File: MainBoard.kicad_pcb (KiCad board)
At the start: 2 copper layers, 121.5 x 73.2 mm, 172 parts, among them J1 CONN_1x4, J10 CONN_2X2, J11 CONN_2X2, J17 HV, J18 CONN_1X2, J19 CONN_1X2, J2 CONN_2X3, J3 CONN_2X3, J4 CONN_2X2, J5 SWDEBUG_CONNECTOR, J6 CONN_2X2, J7 CONN_2X12, J8 CONN_1X2, J9 Micro_SD_Card_Det_Hirose_DM3AT, K1 KT12-1A, K2 G6DN 12V, Q1 SSM3K361TU,LF, Q2 TSM2312, SW1 RESET, U1 VX07805-1000, U10 DCDC_ISO_5V_ISO, U11 STM32G474, U12 M95M56-WMN6P, U13 TS3704IPT, U14 4044, U15 CD4082, U16 ADCMP350, U17 ADG706, U19 TCMT1103, U2 TPS2115A, U23 CD4072BPW, U24 LTC6259, U26 TCMT1103, U27 DCDC_ISO_5V, U28 MIC5365-3.3YC5, U29 Si8900, U3 ld1117s33, U30 MAX14878AWA+, U4 AD8244, U5 MCP2562, U6 LTC6259, U7 ADCMP354, U8 LTC6820, U9 HM2103

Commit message: added a lot of annotations and readability in the schematic, not complete
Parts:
- U12: value M95M56-WMN6P -> M95256-WMN6P
- U14: value 4044 -> CD4044
- U4: value AD8244 -> EL5421T

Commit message: Logo wasn't virtual, new netlist
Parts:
- renumbered G*** to G1, G*** to G2, G*** to G3, G*** to G4

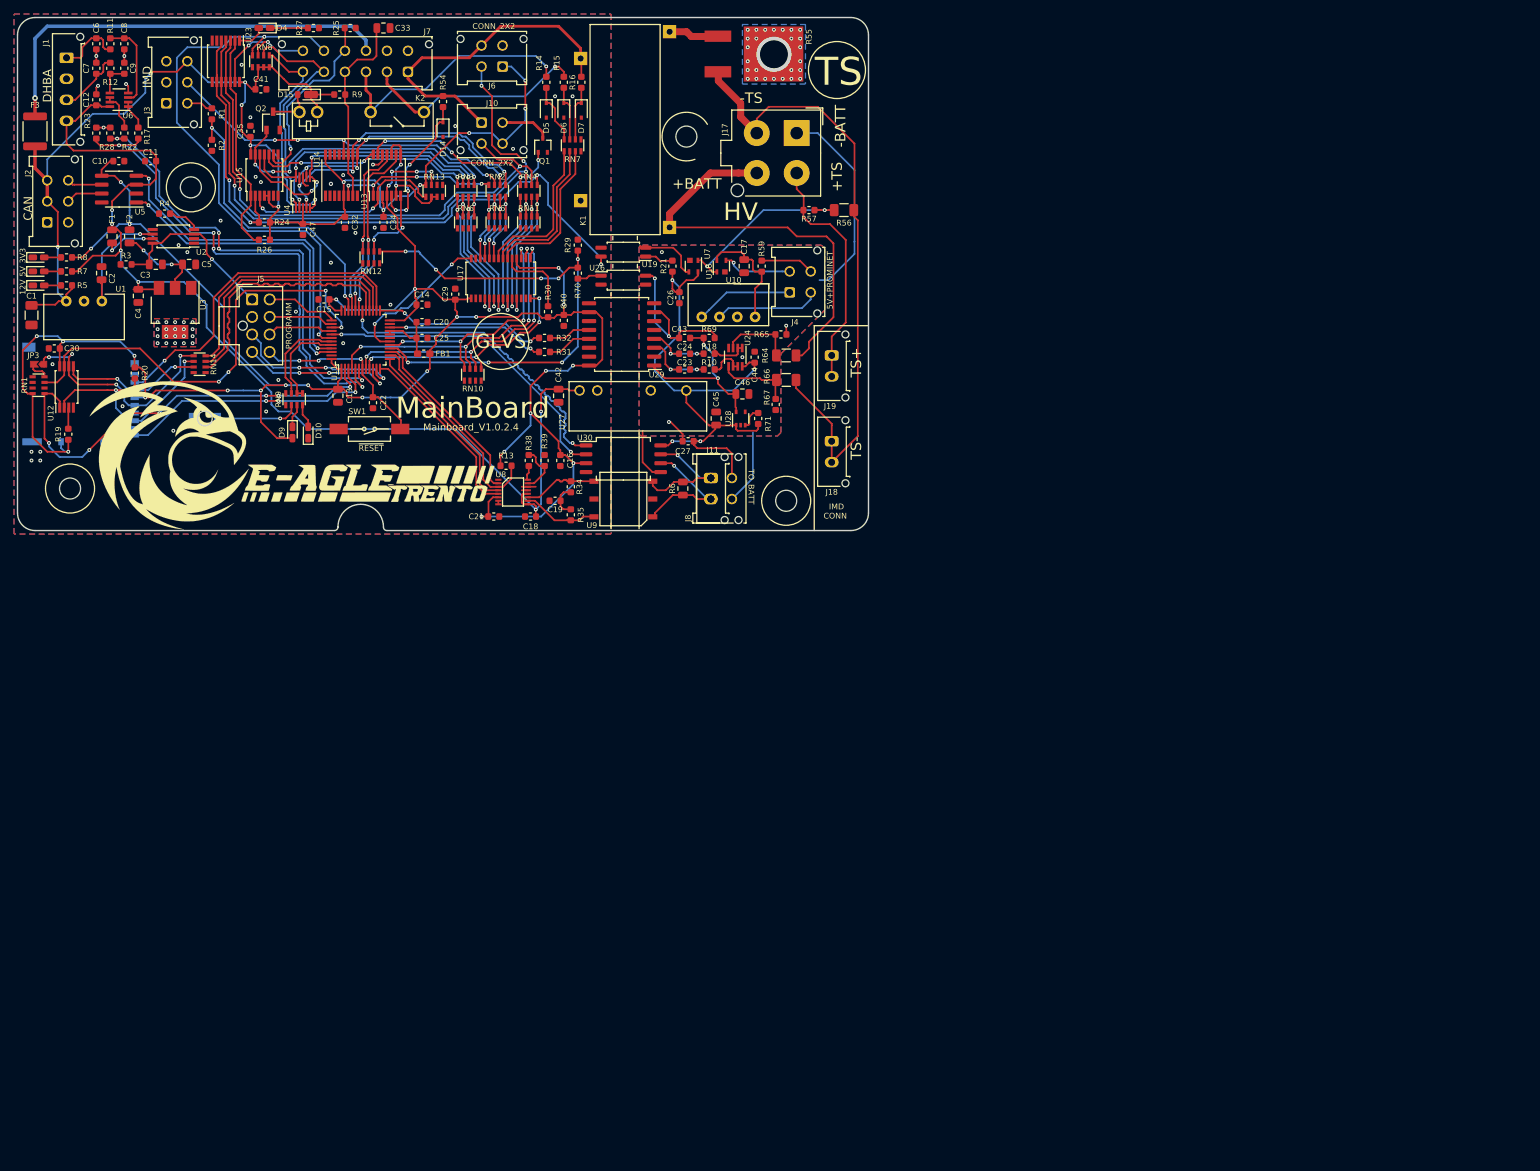
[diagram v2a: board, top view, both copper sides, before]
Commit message: Updated all to the last new v1.0.5 as printed by taba
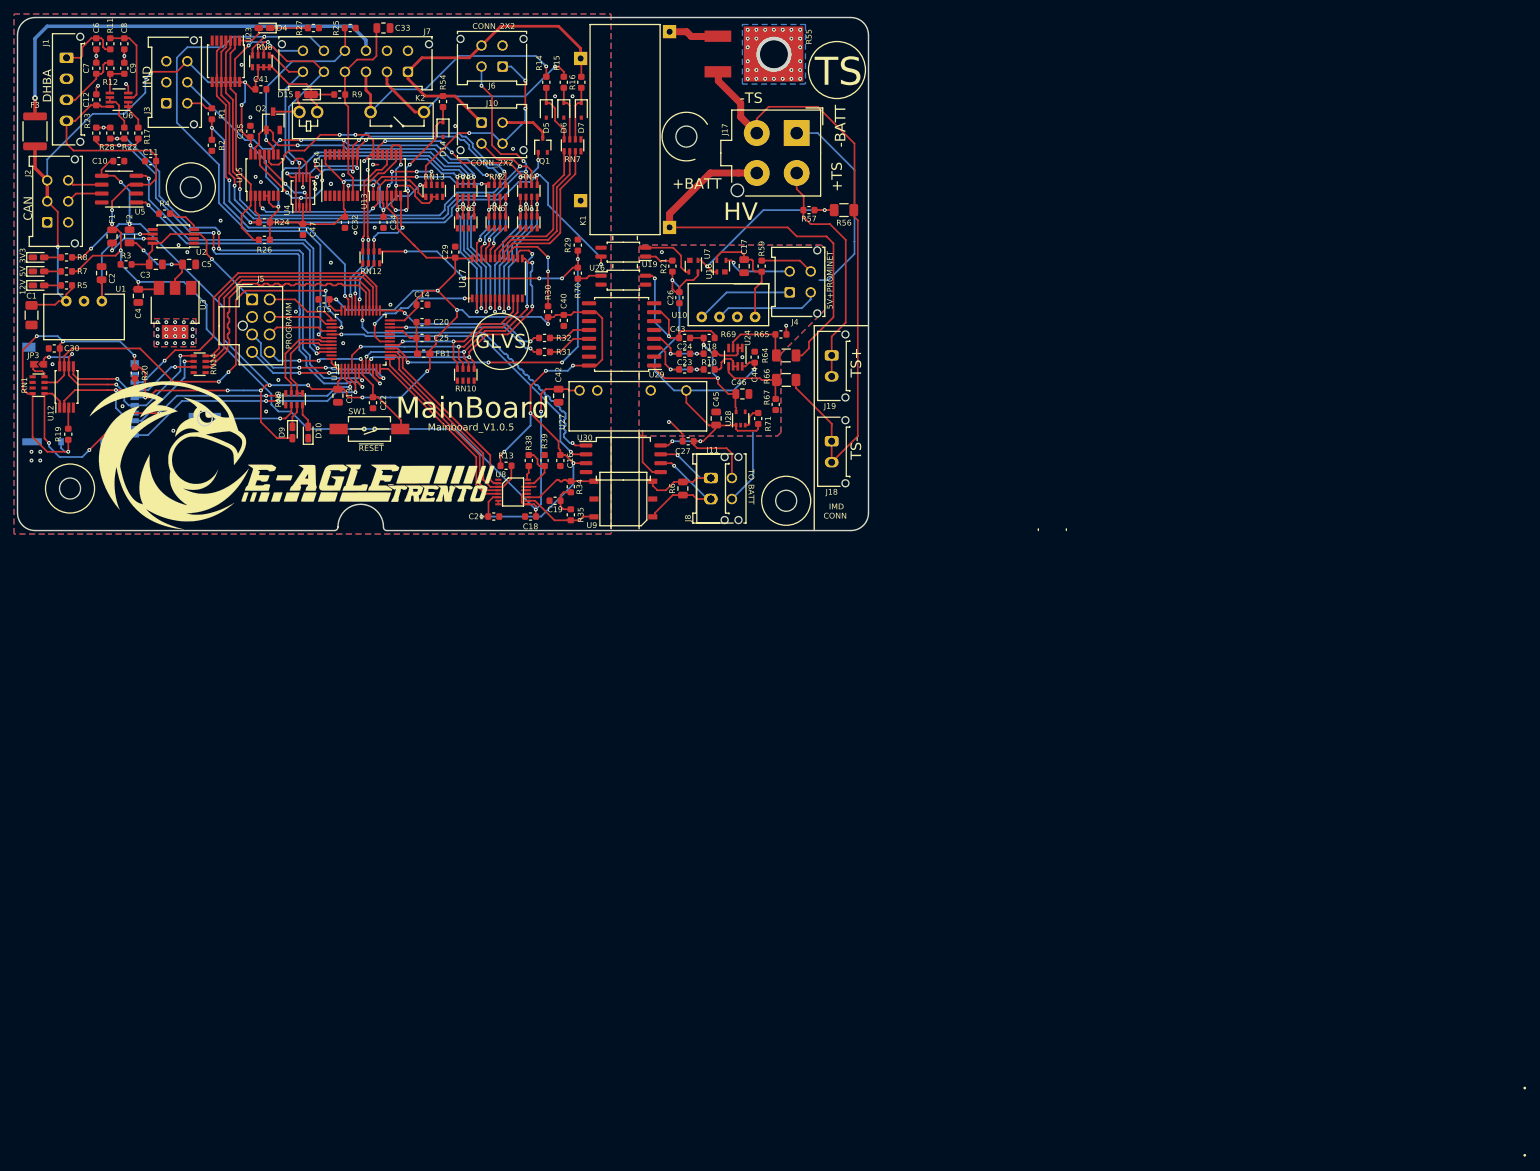
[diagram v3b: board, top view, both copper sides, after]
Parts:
- FB1: value Ferrite_Bead_Small -> FerriteBead_Small
- JP3: value Jumper_NO_Small -> SolderJumper_2_Open
- U17: value ADG706 -> CD74HC4067SM; footprint Package_SO:TSSOP-28_4.4x9.7mm_P0.65mm -> Package_SO:TSSOP-24_4.4x7.8mm_P0.65mm
- U24, U6: value LTC6259 -> LM358
- U4: value EL5421T -> MainBoard_AD8244
- moved C29 6.00 mm to (85.8, 70.5)
- moved RN10 1.00 mm to (87.2, 88.0)
- moved U17 0.50 mm to (91.8, 74.2)
- turned U10 to 0 degrees
- renumbered G2 to G***, G1 to G***, G3 to G***, G4 to G***
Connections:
- U11 pad 17: /AMS/A0 -> /AMS/A2
- U11 pad 8: /AMS/A2 -> /AMS/A0
- U17 pad 1: +3V3 -> /AMS/ANALOG_DATA
- U17 pad 10: /AMS/FB_AIR+ -> /AMS/A2
- U17 pad 11: /AMS/FB_TSAL_OVER60V -> /AMS/A1
- U17 pad 13: Net-(U17-Pad13) -> /AMS/A3
- U17 pad 14: /AMS/A3 -> /AMS/A0
- U17 pad 15: /AMS/A2 -> GND
- U17 pad 16: /AMS/A1 -> /AMS/CHECK_MUX
- U17 pad 17: /AMS/A0 -> /AMS/FB_FROM_TSMS
- U17 pad 18: +3V3 -> /AMS/FB_TO_TSMS
- U17 pad 19: /AMS/CHECK_MUX -> /AMS/FB_FROM_SD
- U17 pad 2: Net-(U17-Pad2) -> /AMS/FB_TS_ON_12V
- U17 pad 20: /AMS/FB_FROM_TSMS -> /AMS/FB_LATCH_IMD
- U17 pad 21: /AMS/FB_TO_TSMS -> /AMS/FB_LATCH_BMS
- U17 pad 22: /AMS/FB_FROM_SD -> /AMS/FB_IMD_FAULT
- U17 pad 23: /AMS/FB_LATCH_IMD -> /AMS/FB_BMS_12V
- U17 pad 24: /AMS/FB_LATCH_BMS -> +3V3
- U17 pad 3: Net-(U17-Pad3) -> /AMS/FB_BMS_SD
- U17 pad 4: /AMS/FB_TS_ON_12V -> /AMS/FB_IMD_SD
- U17 pad 5: /AMS/FB_BMS_SD -> /AMS/FB_RELAY_LV
- U17 pad 6: /AMS/FB_IMD_SD -> /AMS/FB_PC_END_12V
- U17 pad 7: /AMS/FB_RELAY_LV -> /AMS/FB_AIR-
- U17 pad 8: /AMS/FB_PC_END_12V -> /AMS/FB_AIR+
- U17 pad 9: /AMS/FB_AIR- -> /AMS/FB_TSAL_OVER60V
- U4 pad 1: /BMS_LED -> /FB_LACTH_BMS
- U4 pad 10: /FB_IMD_SD -> /FB_LACTH_BMS
- U4 pad 2: /FB_LACTH_BMS -> /FB_BMS_SD
- U4 pad 4: /FB_LACTH_IMD -> /FB_IMD_SD
- U4 pad 5: /IMD_LED -> /FB_LACTH_IMD
- U4 pad 6: /FB_BMS_SD -> /FB_LACTH_IMD
- U4 pad 7: /FB_LACTH_BMS -> /IMD_LED
- U4 pad 9: /FB_LACTH_IMD -> /BMS_LED
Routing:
- net /AMS/A2: track 42.3 -> 25.3 mm, vias 4 -> 2
- net /AMS/A1: track 44.4 -> 33.3 mm, vias 4 -> 2
- net +3V3: track 343.2 -> 335.5 mm, vias 30 -> 28
- net /IMD_LED: track 32.2 -> 24.8 mm
- net /FB_IMD_SD: track 37.5 -> 43.6 mm, vias 2 -> 3
- net /BMS_LED: track 34.1 -> 28.7 mm
- net /FB_TS_ON: track 32.6 -> 37.9 mm, vias 3 -> 4
- net /AMS/A0: track 36.2 -> 41.3 mm
- net /AMS/A3: track 34.1 -> 38.2 mm
- net /FB_SD_MINIRELAY: track 42.4 -> 38.8 mm, vias 4 -> 2
- net /AMS/CHECK_MUX: track 11.1 -> 14.4 mm, vias 0 -> 2
- net /FB_LACTH_IMD: track 44.1 -> 41.7 mm, vias 5 -> 4
- net /AMS/ANALOG_DATA: track 21.9 -> 19.7 mm
- net /FB_BMS_SD: track 41.4 -> 43.6 mm, vias 4 -> 5
- net /AMS/FB_PC_END_12V: track 18.8 -> 20.8 mm
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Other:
- board text added: "Mainboard_V1.0.5"
- board text removed: "Mainboard_V1.0.2.4"
